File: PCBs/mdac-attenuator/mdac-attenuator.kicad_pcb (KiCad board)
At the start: 2 copper layers, 45.7 x 52.1 mm, 34 parts, among them J1 Conn_01x06_Male, J2 Conn_01x06_Male, U1 AD8620, U2 DAC8812ICPWG4

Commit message: Add new text
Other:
- board text added: "MDAC Attenuator v3.0"
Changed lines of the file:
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@@
   (general
     (thickness 1.6)
-    (drawings 26)
+    (drawings 28)
     (tracks 111)
     (zones 0)
@@
     )
   )
+  (gr_text "MDAC\nAttenuator\nv3.0" (at 160.02 78.105) (layer B.SilkS)
+    (effects (font (size 1.143 1.143) (thickness 0.127)) (justify left mirror))
+  )
+  (gr_text "MDAC\nAttenuator\nv3.0" (at 155.575 82.55) (layer F.SilkS)
+    (effects (font (size 1.143 1.143) (thickness 0.127)) (justify left))
+  )
   (gr_text futuresharks@gmail.com (at 124.206 102.362 90) (layer F.SilkS)

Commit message: Misc updates to 3 PCBs
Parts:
- C5_SMD1: footprint Capacitor_SMD:CP_Elec_10x10 -> Capacitor_SMD:CP_Elec_8x10
- moved C5_SMD1 0.19 mm to (161.0, 110.5)
- moved C4 0.06 mm to (144.8, 99.8)
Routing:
- net -15V: track 37.1 -> 35.5 mm
- net +15V: track 31.2 -> 29.9 mm
- net GNDA: vias 1 -> 3

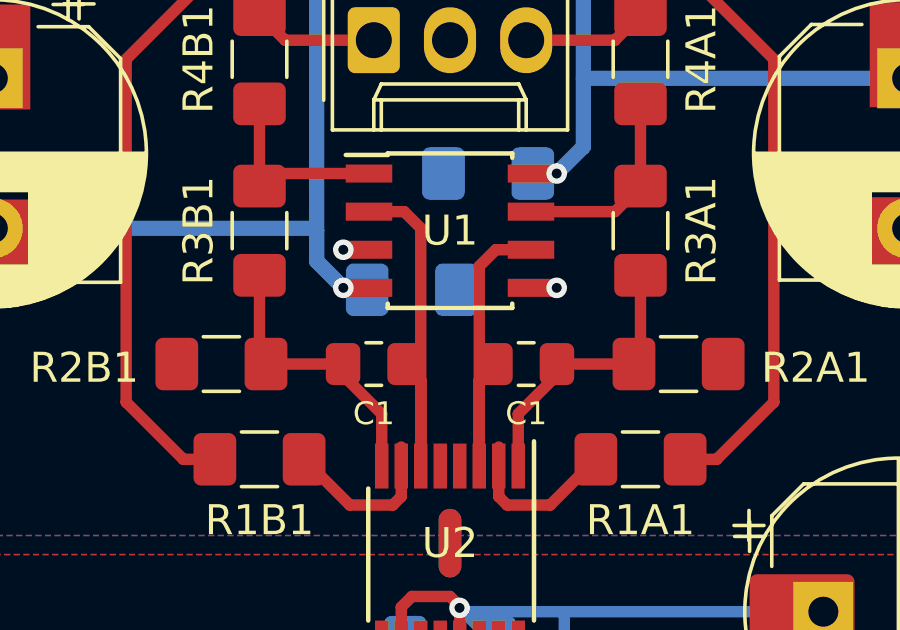
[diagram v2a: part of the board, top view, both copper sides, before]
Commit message: adding BoMs, images and small design updates
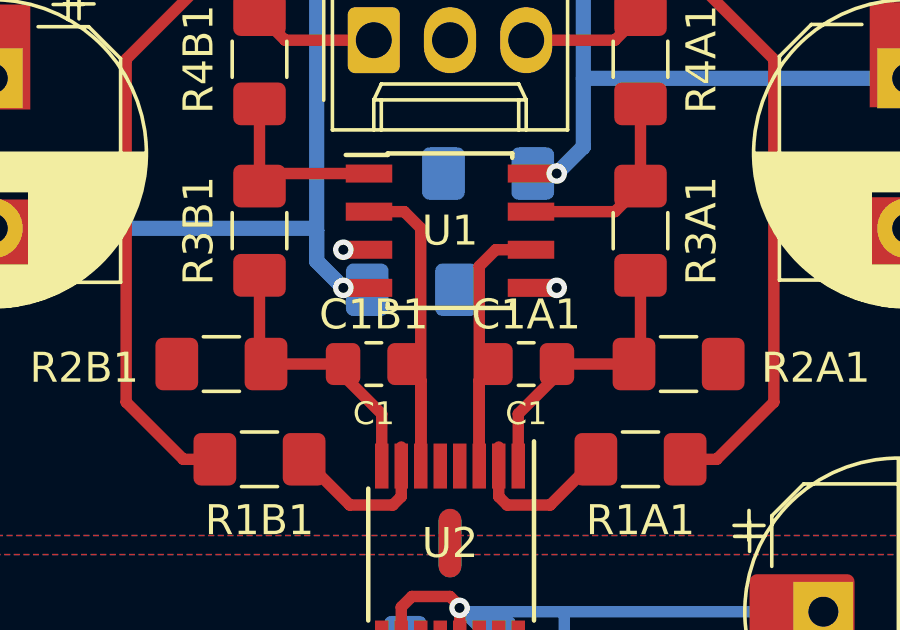
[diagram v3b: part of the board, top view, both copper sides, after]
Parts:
- C1A1, C1B1: footprint Resistor_SMD:R_0805_2012Metric_Pad1.15x1.40mm_HandSolder -> Capacitor_SMD:C_0805_2012Metric_Pad1.15x1.40mm_HandSolder
- C3, C4, C6: footprint Resistor_SMD:R_1206_3216Metric_Pad1.42x1.75mm_HandSolder -> Capacitor_SMD:C_1206_3216Metric_Pad1.42x1.75mm_HandSolder
